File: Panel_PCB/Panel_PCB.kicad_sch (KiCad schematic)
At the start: 94 parts, among them J16 Boton 2, J17 Boton 3, J18 Sensor IN sgn, J19 Sensor OUT sgn, J20 Boton 1, J21 Boton 1 sgn, J22 Sensor IN, J23 Sensor OUT, J24 Boton 2 sgn, J25 Boton 3 sgn, J5 AC, J6 Bateria, K1 SANYOU_SRD_Form_C, K14 SANYOU_SRD_Form_C, K2 SANYOU_SRD_Form_C, K4 EC2-4.5SNU, K8 SANYOU_SRD_Form_C, K9 SANYOU_SRD_Form_C, Q1 Q_NPN, Q2 Q_NPN, Q3 Q_NPN, Q4 Q_NPN, T1 Transformer_1P_1S, U1 TLP291, U15 LM7805_TO220, U16 LM1117T-3.3, U2 TLP291, U20 LM1117T-3.3, U21 LM7812_TO220, U3 TLP291, U4 LM7805_TO220, U5 TLP291, U6 LM7812_TO220

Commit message: Huellas y valores a componentes
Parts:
- added C13: 0.1 μF, Capacitor_THT:C_Disc_D3.0mm_W1.6mm_P2.50mm, symbol Device:C_US
- added J1: Relay 1, TerminalBlock_Phoenix:TerminalBlock_Phoenix_MKDS-1,5-2-5.08_1x02_P5.08mm_Horizontal, symbol Connector:Screw_Terminal_01x02
- added J2: Relay 2, TerminalBlock_Phoenix:TerminalBlock_Phoenix_MKDS-1,5-2-5.08_1x02_P5.08mm_Horizontal, symbol Connector:Screw_Terminal_01x02
- added J3: Relay 3, TerminalBlock_Phoenix:TerminalBlock_Phoenix_MKDS-1,5-2-5.08_1x02_P5.08mm_Horizontal, symbol Connector:Screw_Terminal_01x02
- added J4: Relay 4, TerminalBlock_Phoenix:TerminalBlock_Phoenix_MKDS-1,5-2-5.08_1x02_P5.08mm_Horizontal, symbol Connector:Screw_Terminal_01x02
- C1: value C_US -> 35V 4700μF
- C10, C8: value C -> 100 μF
- C11, C9: value C -> 10 μF
- C12, C2, C4, C6: value C -> 0.22 μF
- C3, C5, C7: value C -> 0.1 μF
- D1: value D_Bridge_+AA- -> KBP204G; footprint Diode_THT:Diode_Bridge_19.0x3.5x10.0mm_P5.0mm -> Diode_THT:Diode_Bridge_Vishay_KBPM
- D2: value D_Zener -> 12 V; footprint Diode_THT:D_A-405_P7.62mm_Horizontal -> Diode_THT:D_DO-41_SOD81_P10.16mm_Horizontal
- F1, F2: footprint (none) -> Fuse:Fuseholder_Cylinder-5x20mm_Schurter_0031_8201_Horizontal_Open
- J16, J17, J18, J19, J20, J21, J22, J23, J24, J25, J5, J6: footprint (none) -> TerminalBlock_Phoenix:TerminalBlock_Phoenix_MKDS-1,5-2-5.08_1x02_P5.08mm_Horizontal
- Q1, Q2, Q3, Q4: footprint (none) -> Package_TO_SOT_THT:TO-92
- R1, R2: value R_US -> 100 Ω 2W; footprint Resistor_THT:R_Axial_DIN0617_L17.0mm_D6.0mm_P30.48mm_Horizontal -> Resistor_THT:R_Axial_DIN0617_L17.0mm_D6.0mm_P25.40mm_Horizontal
- R10, R3, R6, R8: value R_US -> 450; footprint (none) -> Resistor_THT:R_Axial_DIN0207_L6.3mm_D2.5mm_P10.16mm_Horizontal
- R4: footprint (none) -> Resistor_THT:R_Axial_DIN0207_L6.3mm_D2.5mm_P10.16mm_Horizontal
- R5, R7, R9: value R_US -> 150; footprint (none) -> Resistor_THT:R_Axial_DIN0207_L6.3mm_D2.5mm_P10.16mm_Horizontal
- renumbered EN to EN1, VIN to VIN1
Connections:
- net at C1.2, C10.2, C11.2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: now also U1.2, U2.2, U3.2, U5.2, C13.2
- net at K9.1: now also J4.2 (Pin_2)
- net at K9.3: now also J4.1 (Pin_1)
- net at D4.1 (K), D5.1 (K), D6.1 (K)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: now also C13.1
- net at K8.1: now also J1.2 (Pin_2)
- net at K8.3: now also J1.1 (Pin_1)
- net at K2.1: now also J3.2 (Pin_2)
- net at K2.3: now also J3.1 (Pin_1)
- net at K1.1: now also J2.2 (Pin_2)
- net at K1.3: now also J2.1 (Pin_1)
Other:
- moved on the sheet: C3, C6, C7, D2, U4, U6

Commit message: Corrección de errores
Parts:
- removed Q1, Q2, Q3, Q4: Q_NPN, Package_TO_SOT_THT:TO-92, symbol Device:Q_NPN
- removed T1: Transformer_1P_1S, Transformer_THT:Transformer_NF_ETAL_1-1_P1200, symbol Device:Transformer_1P_1S
- added C14: 35V 4700μF, Capacitor_THT:C_Radial_D18.0mm_H35.5mm_P7.50mm, symbol Device:C_US
- added J7, J8: AC, TerminalBlock_Phoenix:TerminalBlock_Phoenix_MKDS-1,5-2-5.08_1x02_P5.08mm_Horizontal, symbol Connector:Screw_Terminal_01x02
- added Q1, Q2, Q3, Q5: 2N2222A, Package_TO_SOT_THT:TO-92, symbol Transistor_BJT:Q_NPN_EBC
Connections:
- net at C1.2, C10.2, C11.2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: now also C14.2
- net at C12.1, C2.1, D2.1 (K)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: now also C1.1
- net at K4.5, R2.1: no longer C1.1
- net at U3.3: now also Q2.2 (B)
- net at D6.2 (A), K1.2: now also Q2.3 (C)
- net at R7.1: now also Q2.1 (E)
- net at D5.2 (A), K9.2: now also Q1.3 (C)
- net at U5.3: now also Q3.2 (B)
- net at D4.2 (A), K8.2: now also Q5.3 (C)
- net at F2.2, K14.2, K4.1: now also J8.1 (Pin_1)
- net at R4.1: now also Q5.1 (E)
- net at K4.4, R1.2: now also C14.1
- net at F1.1: now also J7.2 (Pin_2)
- net at D7.2 (A), K2.2: now also Q3.3 (C)
- net at R9.1: now also Q3.1 (E)
- net at U1.3: now also Q5.2 (B)
- net at U2.3: now also Q1.2 (B)
- net at R5.1: now also Q1.1 (E)
- net at D1.3: now also J7.1 (Pin_1)
- net at J5.1 (Pin_1), K14.5, K4.12: now also J8.2 (Pin_2)
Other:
- note added: "Transformador"
- moved on the sheet: C1, D2, F1, F2, J5, R1, R2

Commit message: Organizando elementos del PCB
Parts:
- R3: renamed from R4; value R_US -> 150
- renumbered C14 to C1, C5 to C10, C10 to C11, C11 to C12, C8 to C13, C9 to C14, C1 to C2, C2 to C3, C3 to C4, C12 to C5, C13 to C6, C6 to C7, C7 to C8, C4 to C9, D4 to D3, D6 to D4, D7 to D5, D5 to D6, D3 to D7, F2 to F1, F1 to F2, J5 to J1, J3 to J10, J4 to J11, J8 to J12, J7 to J13, J18 to J14, J19 to J15, J21 to J16, J24 to J17, J25 to J18, J6 to J2, J22 to J3, J23 to J4, J20 to J5, J16 to J6, J17 to J7, J1 to J8, J2 to J9, K8 to K1, K1 to K2, K2 to K3, K9 to K4, K4 to K5, K14 to K6, Q5 to Q1, Q1 to Q4, R6 to R10, R3 to R4, R7 to R5, R8 to R6, R9 to R7, R10 to R8, R5 to R9, U16 to U10, U3 to U2, U5 to U3, U2 to U4, U6 to U5, U21 to U6, U4 to U7, U15 to U8, U20 to U9
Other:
- moved on the sheet: 3V3, C1, C10, C11, C12, C13, C14, C2, C3, C4, C5, C6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

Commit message: Conexiones al microcontrolador
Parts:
- removed J14: Sensor IN sgn, TerminalBlock_Phoenix:TerminalBlock_Phoenix_MKDS-1,5-2-5.08_1x02_P5.08mm_Horizontal, symbol Connector:Screw_Terminal_01x02
- removed J15: Sensor OUT sgn, TerminalBlock_Phoenix:TerminalBlock_Phoenix_MKDS-1,5-2-5.08_1x02_P5.08mm_Horizontal, symbol Connector:Screw_Terminal_01x02
- removed J16: Boton 1 sgn, TerminalBlock_Phoenix:TerminalBlock_Phoenix_MKDS-1,5-2-5.08_1x02_P5.08mm_Horizontal, symbol Connector:Screw_Terminal_01x02
- removed J17: Boton 2 sgn, TerminalBlock_Phoenix:TerminalBlock_Phoenix_MKDS-1,5-2-5.08_1x02_P5.08mm_Horizontal, symbol Connector:Screw_Terminal_01x02
- removed J18: Boton 3 sgn, TerminalBlock_Phoenix:TerminalBlock_Phoenix_MKDS-1,5-2-5.08_1x02_P5.08mm_Horizontal, symbol Connector:Screw_Terminal_01x02
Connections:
- net at GPIO35.1 (Pin_1): now also C12.1, GPIO34.1 (Pin_1), J3.2 (Pin_2), J4.2 (Pin_2), U9.2 (VO)
- net at C14.1, U10.2 (VO): now also GPIO14.1 (Pin_1), GPIO26.1 (Pin_1), GPIO27.1 (Pin_1), J5.2 (Pin_2), J6.2 (Pin_2), J7.2 (Pin_2)
- net at U2.1: now also GPIO32.1 (Pin_1)
- net at U3.1: now also GPIO33.1 (Pin_1)
- net at U4.1: now also GPIO25.1 (Pin_1)
- net at U1.1: now also GPIO23.1 (Pin_1)
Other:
- note added: "12 VDC"
- note added: "120 VAC"
- note added: "Boton 1"
- note added: "Boton 2"
- note added: "Boton 3"
- note added: "Relay 1"
- note added: "Relay 2"
- note added: "Relay 3"
- note added: "Relay 4"
- note added: "Sensor entrada"
- note added: "Sensor salida"
- note removed: "Señales de voltaje para el microcontrolador"
- moved on the sheet: 3V3, C1, C10, C11, C12, C13, C14, C2, C3, C4, C5, C6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

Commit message: Actualización de PCB
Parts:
- added D8, D9: 1N4001, Diode_THT:D_DO-41_SOD81_P10.16mm_Horizontal, symbol Diode:1N4001
- added R11, R12, R13, R14: 1000, Resistor_THT:R_Axial_DIN0207_L6.3mm_D2.5mm_P10.16mm_Horizontal, symbol Device:R_US
- R10, R4, R6, R8: value 450 -> 500
- R3, R5, R7, R9: value 150 -> 100
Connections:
- net at Q4.2 (B): now also R14.2; no longer U4.3
- net at C4.1, C7.1, C9.1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: now also K6.4, D8.1 (K); no longer K6.3, U5.3 (VO)
- net at Q1.2 (B): now also R11.1; no longer U1.3
- net at U2.3: now also R12.1; no longer Q2.2 (B)
- net at C6.1, D3.1 (K), D4.1 (K)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: now also D9.1 (K); no longer U6.3 (VO)
- net at U3.3: now also R13.1; no longer Q3.2 (B)
- new net: D8.2 (A), U5.3 (VO)
- new net: Q2.2 (B), R12.2
- new net: R14.1, U4.3
- new net: R11.2, U1.3
- new net: D9.2 (A), U6.3 (VO)
- new net: Q3.2 (B), R13.2
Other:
- moved on the sheet: C10, C11, C12, C13, C14, C4, C6, C7, C8, C9, D3, D4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

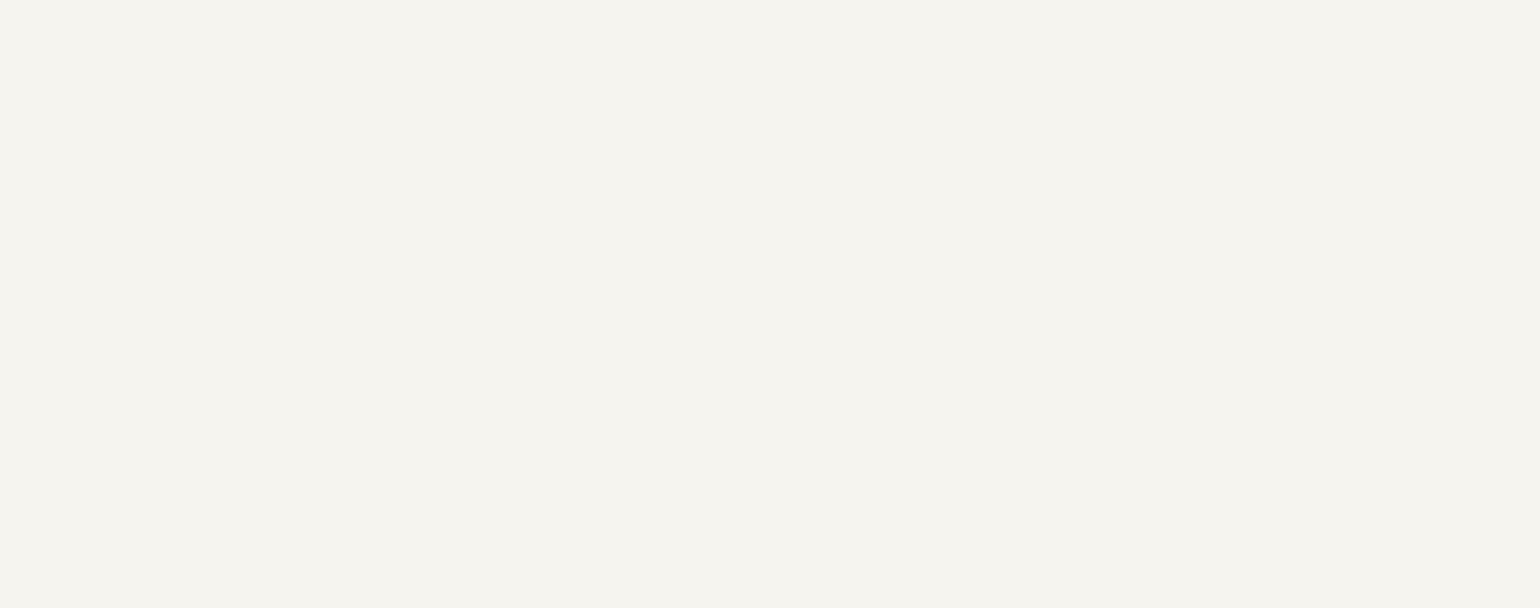
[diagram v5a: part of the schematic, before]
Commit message: Circuitos para detectar bateria descargada y circuito para cargar la batería
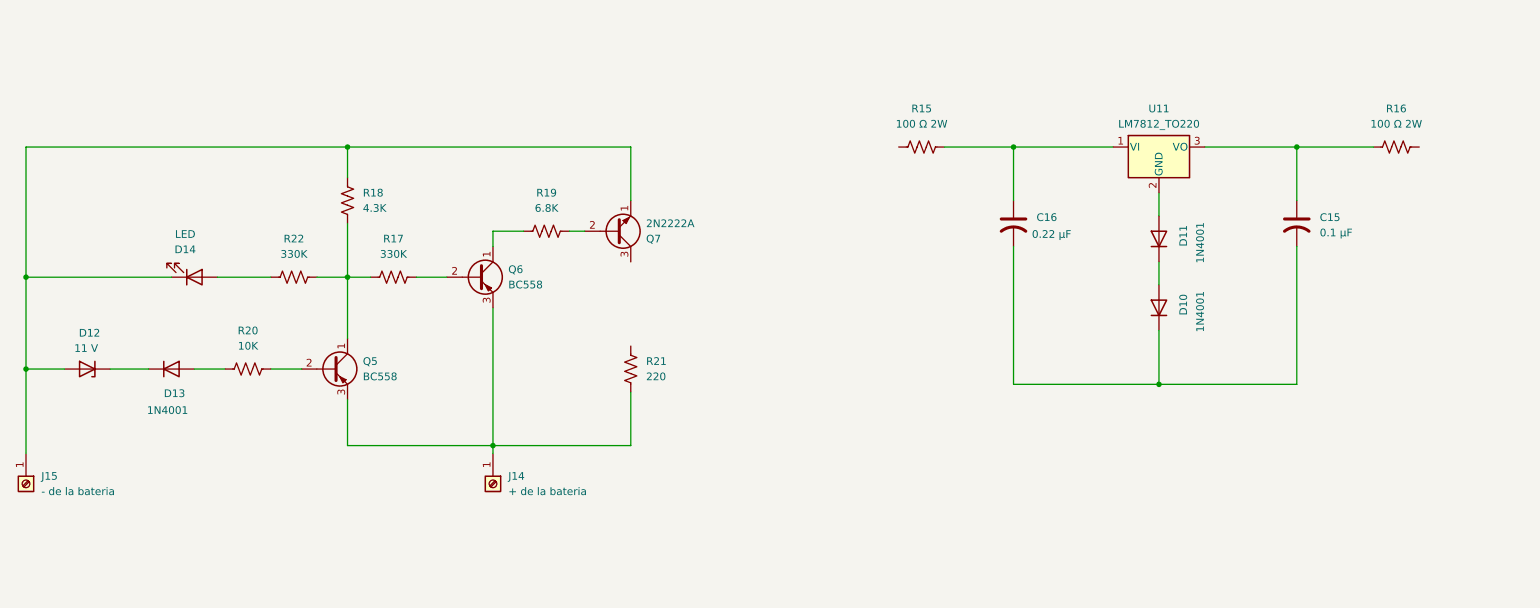
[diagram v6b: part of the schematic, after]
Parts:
- added C15: 0.1 μF, Capacitor_THT:C_Disc_D3.0mm_W1.6mm_P2.50mm, symbol Device:C_US
- added C16: 0.22 μF, Capacitor_THT:C_Disc_D3.0mm_W1.6mm_P2.50mm, symbol Device:C_US
- added D10, D11, D13: 1N4001, Diode_THT:D_DO-41_SOD81_P10.16mm_Horizontal, symbol Diode:1N4001
- added D12: 11 V, Diode_THT:D_DO-41_SOD81_P10.16mm_Horizontal, symbol Device:D_Zener
- added D14: LED, symbol Device:LED
- added J14: + de la bateria, symbol Connector:Screw_Terminal_01x01
- added J15: - de la bateria, symbol Connector:Screw_Terminal_01x01
- added Q5, Q6: BC558, Package_TO_SOT_THT:TO-92_Inline, symbol Transistor_BJT:BC558
- added Q7: 2N2222A, Package_TO_SOT_THT:TO-92, symbol Transistor_BJT:Q_NPN_EBC
- added R15, R16: 100 Ω 2W, Resistor_THT:R_Axial_DIN0617_L17.0mm_D6.0mm_P25.40mm_Horizontal, symbol Device:R_US
- added R17, R22: 330K, Resistor_THT:R_Axial_DIN0309_L9.0mm_D3.2mm_P12.70mm_Horizontal, symbol Device:R_US
- added R18: 4.3K, Resistor_THT:R_Axial_DIN0309_L9.0mm_D3.2mm_P12.70mm_Horizontal, symbol Device:R_US
- added R19: 6.8K, Resistor_THT:R_Axial_DIN0309_L9.0mm_D3.2mm_P12.70mm_Horizontal, symbol Device:R_US
- added R20: 10K, Resistor_THT:R_Axial_DIN0309_L9.0mm_D3.2mm_P12.70mm_Horizontal, symbol Device:R_US
- added R21: 220, Resistor_THT:R_Axial_DIN0309_L9.0mm_D3.2mm_P12.70mm_Horizontal, symbol Device:R_US
- added U11: LM7812_TO220, Package_TO_SOT_THT:TO-220-3_Vertical, symbol Regulator_Linear:LM7812_TO220
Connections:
- new net: C15.1, R16.1, U11.3 (VO)
- new net: C15.2, C16.2, D10.1 (K)
- new net: Q6.1 (C), R19.2
- new net: Q6.2 (B), R17.1
- new net: J14.1 (Pin_1), Q5.3 (E), Q6.3 (E), R21.2
- new net: D12.1 (K), D13.1 (K)
- new net: D12.2 (A), D14.1 (K), J15.1 (Pin_1), Q7.1 (E), R18.1
- new net: Q5.1 (C), R17.2, R18.2, R22.1
- new net: Q5.2 (B), R20.1
- new net: D13.2 (A), R20.2
- new net: Q7.2 (B), R19.1
- new net: D10.2 (A), D11.1 (K)
- new net: D11.2 (A), U11.2 (GND)
- new net: C16.1, R15.2, U11.1 (VI)
- new net: D14.2 (A), R22.2

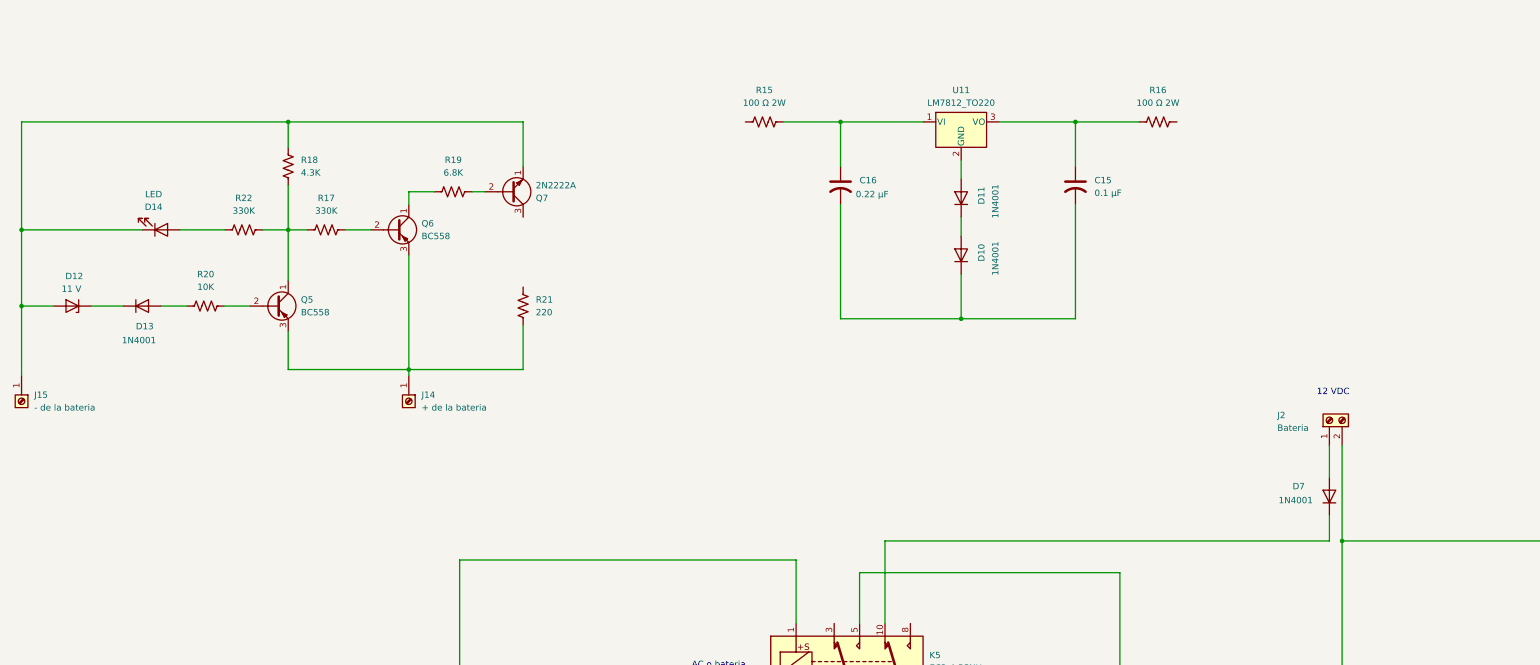
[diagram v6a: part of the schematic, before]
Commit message: Analisis de circuitos para detección de voltaje y carga de bateria
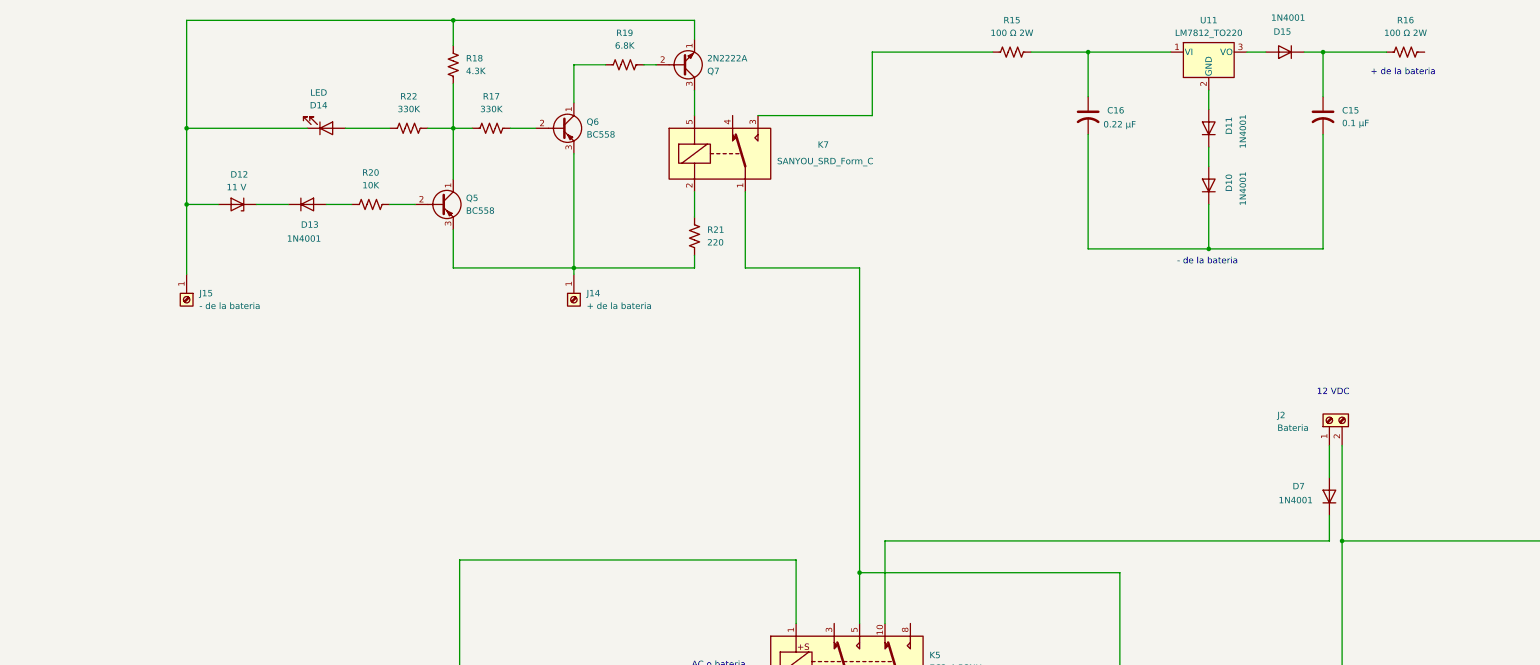
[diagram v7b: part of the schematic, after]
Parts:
- added D15: 1N4001, Diode_THT:D_DO-41_SOD81_P10.16mm_Horizontal, symbol Diode:1N4001
- added K7: SANYOU_SRD_Form_C, Relay_THT:Relay_SPDT_SANYOU_SRD_Series_Form_C, symbol Relay:SANYOU_SRD_Form_C
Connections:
- net at C15.1, R16.1: now also D15.1 (K); no longer U11.3 (VO)
- net at R21.1: now also K7.2
- net at K5.5, R2.1: now also K7.1
- net at Q7.3 (C): now also K7.5
- net at R15.1: now also K7.3
- new net: D15.2 (A), U11.3 (VO)
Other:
- note added: "+ de la bateria"
- note added: "- de la bateria"
- moved on the sheet: C15, C16, D10, D11, D12, D13, D14, J14, J15, Q5, Q6, Q7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
